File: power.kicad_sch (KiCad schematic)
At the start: 62 parts, among them IC10 TPS7A3001DGNT, IC11 ADP150AUJZ-3.3-R7, IC4 ADP150AUJZ-3.3-R7, IC5 ADP150AUJZ-3.3-R7, IC6 ADP150AUJZ-3.3-R7, IC7 ADP150AUJZ-3.3-R7, IC8 LT1026CS8#PBF, IC9 ADP7118ARDZ

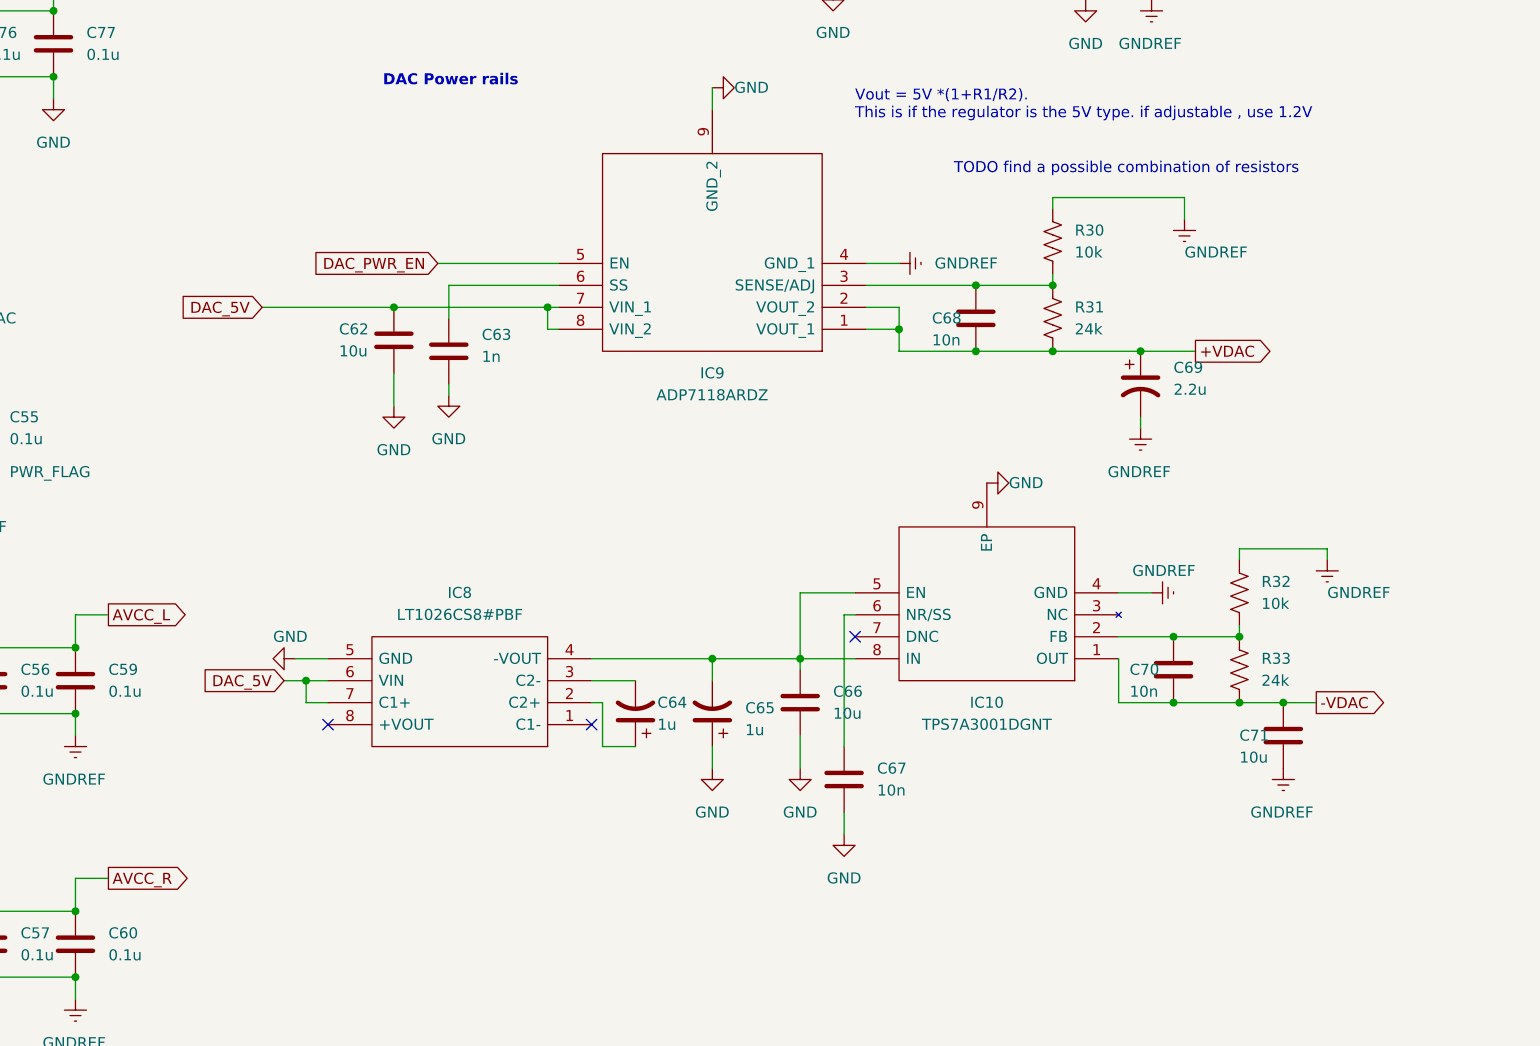
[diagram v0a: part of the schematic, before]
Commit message: Changing negative rail power supply
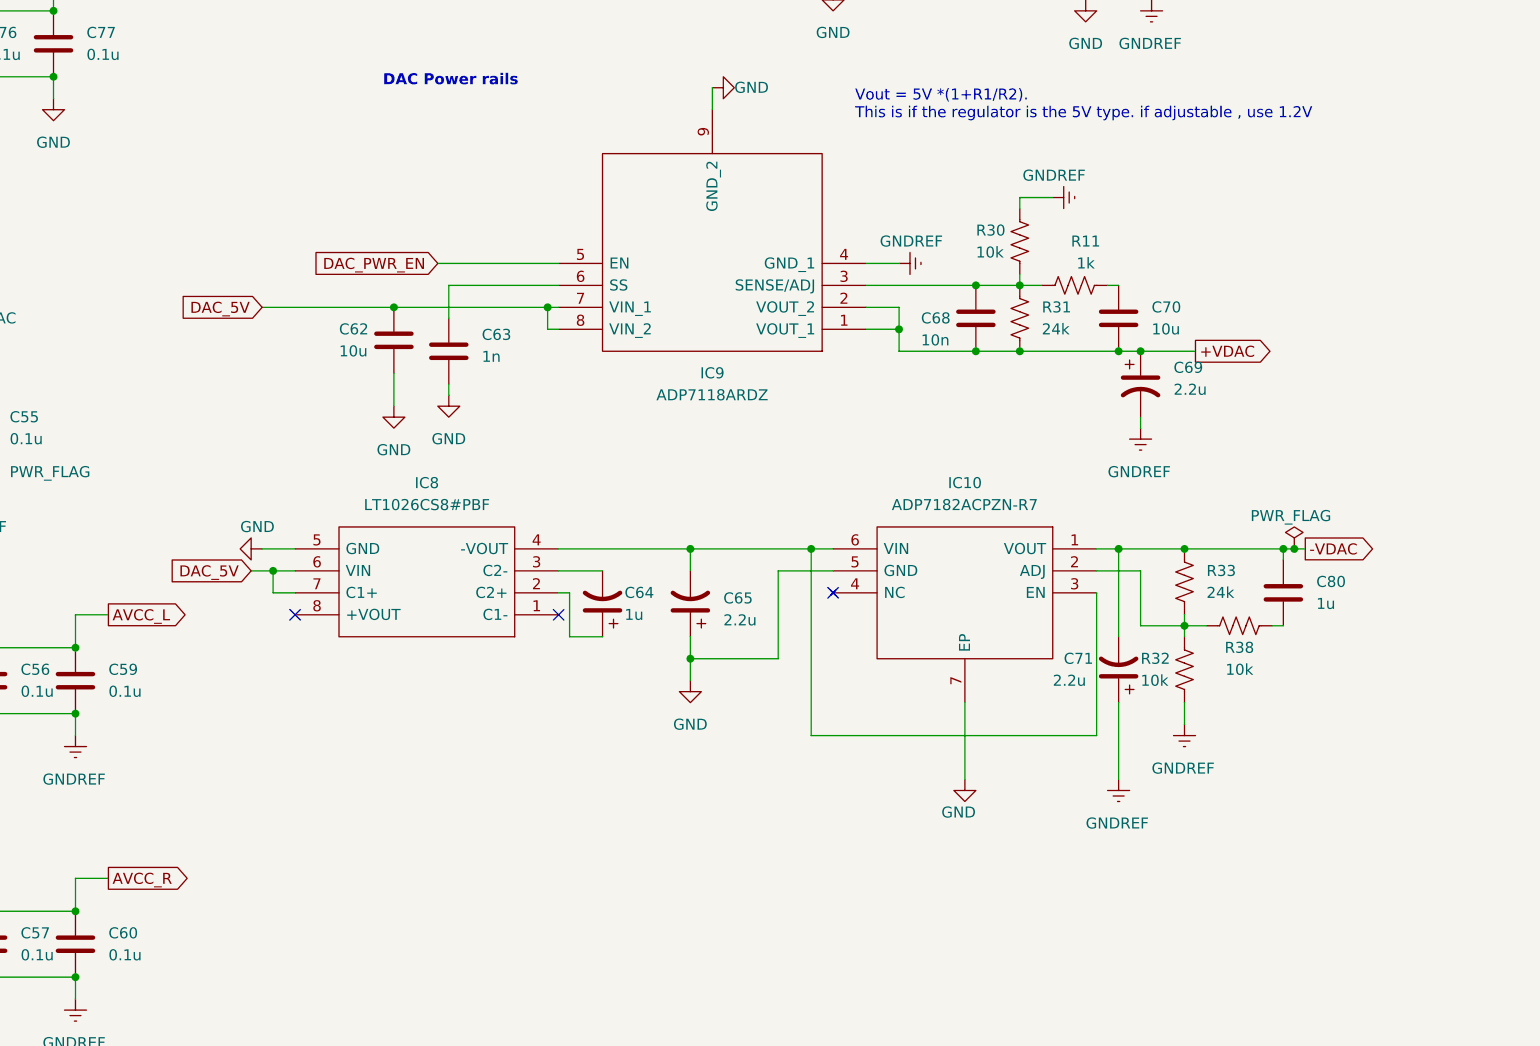
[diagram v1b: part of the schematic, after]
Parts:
- removed C66, C71: 10u, Capacitor_SMD:C_0805_2012Metric_Pad1.18x1.45mm_HandSolder, symbol Device:C
- removed C67: 10n, Capacitor_SMD:C_0805_2012Metric_Pad1.18x1.45mm_HandSolder, symbol Device:C
- removed IC10: TPS7A3001DGNT, SamacSys_Parts:SOP65P490X110-9N, symbol SamacSys_Parts:TPS7A3001DGNT
- added C71: 2.2u, Capacitor_THT:CP_Radial_D4.0mm_P1.50mm, symbol Device:C_Polarized_US
- added C80: 1u, Capacitor_SMD:C_0805_2012Metric_Pad1.18x1.45mm_HandSolder, symbol Device:C
- added IC10: ADP7182ACPZN-R7, SON65P200X200X65-7N-D, symbol SamacSys_Parts:ADP7182ACPZN-R7
- added R11: 1k, Resistor_SMD:R_0805_2012Metric_Pad1.20x1.40mm_HandSolder, symbol Device:R_US
- added R38: 10k, Resistor_SMD:R_0805_2012Metric_Pad1.20x1.40mm_HandSolder, symbol Device:R_US
- C65: value 1u -> 2.2u; footprint Capacitor_THT:CP_Radial_D5.0mm_P2.00mm -> Capacitor_THT:CP_Radial_D4.0mm_P1.50mm; Mouser Part Number 80-ESH105M100AC3AA -> 667-ECE-A1HKA2R2; Part Number ESH105M100AC3AA -> ECE-A1HKA2R2
- C70: value 10n -> 10u; Mouser Part Number 80-C0805C103K4RECTU -> 963-LMK212ABJ106KG8T; Part Number C0805C103K4RECTU -> LMK212ABJ106KG8T
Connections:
- net +VDAC: now also C70.2
- net -VDAC: now also R33.2, C71.2, C80.1, IC10.1 (VOUT); no longer C70.2, R33.1
- net GND: now also IC10.5 (GND), IC10.7 (EP)
- net GNDREF: now also R32.1, C71.1; no longer R32.2
- net at C65.2, IC8.4 (-VOUT): now also IC10.3 (EN), IC10.6 (VIN)
- net at C68.1, IC9.3 (SENSE/ADJ), R30.1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: now also R11.1
- new net: C70.1, R11.2
- new net: IC10.2 (ADJ), R32.2, R33.1, R38.2
- new net: C80.2, R38.1
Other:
- note removed: "TODO find a possible combination of resistors"
- moved on the sheet: C64, IC8, R30, R31, R32, R33

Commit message: updates
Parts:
- added C66: 4.7u, Capacitor_SMD:C_0805_2012Metric_Pad1.18x1.45mm_HandSolder, symbol Device:C
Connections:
- net DAC_5V: now also C66.2
- net GND: now also C66.1
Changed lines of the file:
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@@
   (junction (at 118.11 36.83) (diameter 0) (color 0 0 0 0)
   )
+  (junction (at 153.67 128.27) (diameter 0) (color 0 0 0 0)
+  )
   (junction (at 110.49 167.64) (diameter 0) (color 0 0 0 0)
   )
@@
   )
   (junction (at 236.22 95.25) (diameter 0) (color 0 0 0 0)
+  )
+  (junction (at 153.67 120.65) (diameter 0) (color 0 0 0 0)
   )
   (junction (at 106.68 63.5) (diameter 0) (color 0 0 0 0)
@@
     (stroke (width 0) (type default) (color 0 0 0 0))
   )
+  (wire (pts (xy 153.67 128.27) (xy 154.94 128.27))
+    (stroke (width 0) (type default) (color 0 0 0 0))
+  )
   (wire (pts (xy 118.11 36.83) (xy 129.54 36.83))
     (stroke (width 0) (type default) (color 0 0 0 0))
@@
     (stroke (width 0) (type default) (color 0 0 0 0))
   )
+  (wire (pts (xy 147.32 120.65) (xy 153.67 120.65))
+    (stroke (width 0) (type default) (color 0 0 0 0))
+  )
   (wire (pts (xy 241.3 85.09) (xy 245.11 85.09))
     (stroke (width 0) (type default) (color 0 0 0 0))
@@
     (stroke (width 0) (type default) (color 0 0 0 0))
   )
+  (wire (pts (xy 157.48 125.73) (xy 157.48 120.65))
+    (stroke (width 0) (type default) (color 0 0 0 0))
+  )
   (wire (pts (xy 255.27 102.87) (xy 261.62 102.87))
     (stroke (width 0) (type default) (color 0 0 0 0))
@@
     (stroke (width 0) (type default) (color 0 0 0 0))
   )
+  (wire (pts (xy 157.48 120.65) (xy 153.67 120.65))
+    (stroke (width 0) (type default) (color 0 0 0 0))
+  )
   (wire (pts (xy 59.69 167.64) (xy 41.91 167.64))
     (stroke (width 0) (type default) (color 0 0 0 0))
@@
     (stroke (width 0) (type default) (color 0 0 0 0))
   )
-  (wire (pts (xy 152.4 128.27) (xy 154.94 128.27))
+  (wire (pts (xy 152.4 128.27) (xy 153.67 128.27))
     (stroke (width 0) (type default) (color 0 0 0 0))
   )
@@
   )
   (wire (pts (xy 223.52 95.25) (xy 236.22 95.25))
-    (stroke (width 0) (type default) (color 0 0 0 0))
-  )
-  (wire (pts (xy 153.67 125.73) (xy 157.48 125.73))
     (stroke (width 0) (type default) (color 0 0 0 0))
   )
@@
     )
     (property "Part Number" "LMK212ABJ106KG8T" (id 5) (at 252.73 99.06 0)
+      (effects (font (size 1.27 1.27)) hide)
+    )
+    (pin "1")
+    (pin "2")
+  )
+  (symbol (lib_id "Device:C") (at 153.67 124.46 0) (unit 1)
+    (in_bom yes) (on_board yes)
+    (property "Reference" "C66" (id 0) (at 148.59 121.92 0)
+      (effects (font (size 1.27 1.27)) (justify left))
+    )
+    (property "Value" "4.7u" (id 1) (at 146.05 124.46 0)
+      (effects (font (size 1.27 1.27)) (justify left))
+    )
+    (property "Footprint" "Capacitor_SMD:C_0805_2012Metric_Pad1.18x1.45mm_HandSolder" (id 2) (at 154.6352 128.27 0)
+      (effects (font (size 1.27 1.27)) hide)
+    )
+    (property "Datasheet" "~" (id 3) (at 153.67 124.46 0)
+      (effects (font (size 1.27 1.27)) hide)
+    )
+    (property "Part Number" "C0805C104K8RACAUTO" (id 4) (at 153.67 124.46 0)
+      (effects (font (size 1.27 1.27)) hide)
+    )
+    (property "Mouser Part Number" "80-C0805C104K8RAUTO" (id 5) (at 153.67 124.46 0)
       (effects (font (size 1.27 1.27)) hide)
     )
@@
     (pin "2")
   )
-  (symbol (lib_id "power:GND") (at 153.67 125.73 270) (unit 1)
+  (symbol (lib_id "power:GND") (at 147.32 120.65 270) (unit 1)
     (in_bom yes) (on_board yes)
-    (property "Reference" "#PWR0162" (id 0) (at 147.32 125.73 0)
-      (effects (font (size 1.27 1.27)) hide)
-    )
-    (property "Value" "GND" (id 1) (at 151.13 123.19 90)
-      (effects (font (size 1.27 1.27)) (justify left))
-    )
-    (property "Footprint" "" (id 2) (at 153.67 125.73 0)
-      (effects (font (size 1.27 1.27)) hide)
-    )
-    (property "Datasheet" "" (id 3) (at 153.67 125.73 0)
-      (effects (font (size 1.27 1.27)) hide)
-    )
+    (property "Reference" "#PWR0162" (id 0) (at 140.97 120.65 0)
+      (effects (font (size 1.27 1.27)) hide)
+    )
+    (property "Value" "GND" (id 1) (at 144.78 118.11 90)
+      (effects (font (size 1.27 1.27)) (justify left))
+    )
+    (property "Footprint" "" (id 2) (at 147.32 120.65 0)
+      (effects (font (size 1.27 1.27)) hide)
+    )
+    (property "Datasheet" "" (id 3) (at 147.32 120.65 0)
+      (effects (font (size 1.27 1.27)) hide)
+    )
